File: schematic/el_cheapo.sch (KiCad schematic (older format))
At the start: 5 parts

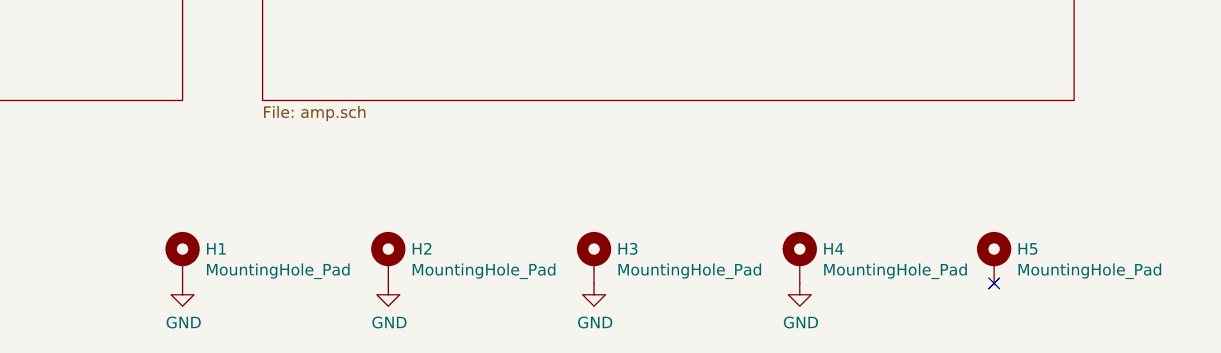
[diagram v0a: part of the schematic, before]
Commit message: altered boards to fit dynaco amps of a similar design.
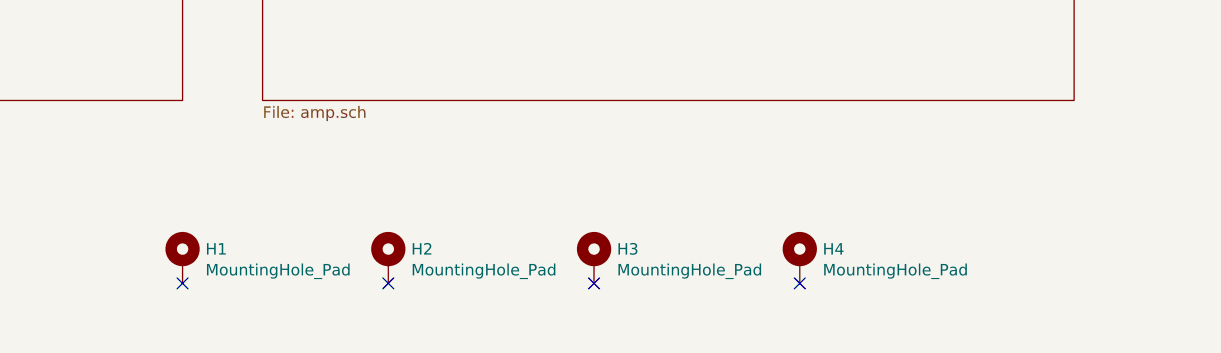
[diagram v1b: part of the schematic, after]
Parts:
- removed H5: MountingHole_Pad, MountingHole:MountingHole_3.2mm_M3_Pad, symbol Mechanical:MountingHole_Pad
- H1, H2: footprint MountingHole:MountingHole_3.2mm_M3_Pad -> MountingHole:MountingHole_4.3x6.2mm_M4_Pad
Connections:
- removed net GND: H1.1, H2.1, H3.1, H4.1
- no-connect marks 1 -> 4
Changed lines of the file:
@@
 	5700 3950 5350 3950
-$Comp
-L Mechanical:MountingHole_Pad H5
-U 1 1 5FF6D28D
-P 8900 5700
-F 0 "H5" H 9000 5749 50  0000 L CNN
-F 1 "MountingHole_Pad" H 9000 5658 50  0000 L CNN
-F 2 "MountingHole:MountingHole_3.2mm_M3_Pad" H 8900 5700 50  0001 C CNN
-F 3 "~" H 8900 5700 50  0001 C CNN
-	1    8900 5700
-	1    0    0    -1
-$EndComp
 $Comp
 L Mechanical:MountingHole_Pad H4
@@
 F 0 "H2" H 6350 5749 50  0000 L CNN
 F 1 "MountingHole_Pad" H 6350 5658 50  0000 L CNN
-F 2 "MountingHole:MountingHole_3.2mm_M3_Pad" H 6250 5700 50  0001 C CNN
+F 2 "MountingHole:MountingHole_4.3x6.2mm_M4_Pad" H 6250 5700 50  0001 C CNN
 F 3 "~" H 6250 5700 50  0001 C CNN
 	1    6250 5700
@@
 F 0 "H1" H 5450 5749 50  0000 L CNN
 F 1 "MountingHole_Pad" H 5450 5658 50  0000 L CNN
-F 2 "MountingHole:MountingHole_3.2mm_M3_Pad" H 5350 5700 50  0001 C CNN
+F 2 "MountingHole:MountingHole_4.3x6.2mm_M4_Pad" H 5350 5700 50  0001 C CNN
 F 3 "~" H 5350 5700 50  0001 C CNN
 	1    5350 5700
 	1    0    0    -1
 $EndComp
-$Comp
-L power:GND #PWR01
-U 1 1 5FF7B5BA
-P 5350 5800
-F 0 "#PWR01" H 5350 5550 50  0001 C CNN
-F 1 "GND" H 5355 5627 50  0000 C CNN
-F 2 "" H 5350 5800 50  0001 C CNN
-F 3 "" H 5350 5800 50  0001 C CNN
-	1    5350 5800
-	1    0    0    -1
-$EndComp
-$Comp
-L power:GND #PWR02
-U 1 1 5FF7B7FD
-P 6250 5800
-F 0 "#PWR02" H 6250 5550 50  0001 C CNN
-F 1 "GND" H 6255 5627 50  0000 C CNN
-F 2 "" H 6250 5800 50  0001 C CNN
-F 3 "" H 6250 5800 50  0001 C CNN
-	1    6250 5800
-	1    0    0    -1
-$EndComp
-$Comp
-L power:GND #PWR03
-U 1 1 5FF7BAAE
-P 7150 5800
-F 0 "#PWR03" H 7150 5550 50  0001 C CNN
-F 1 "GND" H 7155 5627 50  0000 C CNN
-F 2 "" H 7150 5800 50  0001 C CNN
-F 3 "" H 7150 5800 50  0001 C CNN
-	1    7150 5800
-	1    0    0    -1
-$EndComp
-$Comp
-L power:GND #PWR04
-U 1 1 5FF7BB99
-P 8050 5800
-F 0 "#PWR04" H 8050 5550 50  0001 C CNN
-F 1 "GND" H 8055 5627 50  0000 C CNN
-F 2 "" H 8050 5800 50  0001 C CNN
-F 3 "" H 8050 5800 50  0001 C CNN
-	1    8050 5800
-	1    0    0    -1
-$EndComp
-NoConn ~ 8900 5800
+NoConn ~ 8050 5800
+NoConn ~ 7150 5800
+NoConn ~ 6250 5800
+NoConn ~ 5350 5800
 $EndSCHEMATC

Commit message: updated dynaco footprint. First try wasn't perfect. This offers some flexability by using oblong holes.
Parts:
- H3, H4: footprint MountingHole:MountingHole_3.2mm_M3_Pad -> MountingHole:MountingHole_4.3x6.2mm_M4_Pad
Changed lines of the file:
@@
 F 0 "H4" H 8150 5749 50  0000 L CNN
 F 1 "MountingHole_Pad" H 8150 5658 50  0000 L CNN
-F 2 "MountingHole:MountingHole_3.2mm_M3_Pad" H 8050 5700 50  0001 C CNN
+F 2 "MountingHole:MountingHole_4.3x6.2mm_M4_Pad" H 8050 5700 50  0001 C CNN
 F 3 "~" H 8050 5700 50  0001 C CNN
 	1    8050 5700
@@
 F 0 "H3" H 7250 5749 50  0000 L CNN
 F 1 "MountingHole_Pad" H 7250 5658 50  0000 L CNN
-F 2 "MountingHole:MountingHole_3.2mm_M3_Pad" H 7150 5700 50  0001 C CNN
+F 2 "MountingHole:MountingHole_4.3x6.2mm_M4_Pad" H 7150 5700 50  0001 C CNN
 F 3 "~" H 7150 5700 50  0001 C CNN
 	1    7150 5700
